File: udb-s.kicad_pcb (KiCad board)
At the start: 4 copper layers, 40 x 9 mm, 11 parts, among them J1 TYPE-C-31-M-12, J2 78171-0004, U1 TPD4E05U06DQAR

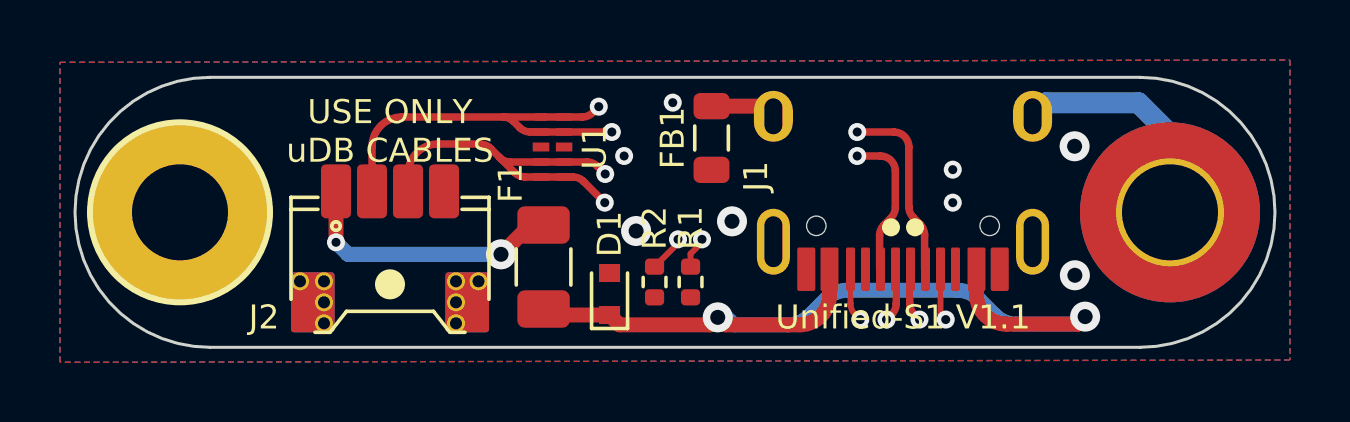
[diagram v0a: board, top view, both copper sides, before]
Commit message: Changed the Pinout of the ezMate connector. Added panelization with KiKit. 2x5 panels is about as small as possible for PCBA at JLCPCB, they want 70x70mm minimal size of the PCB. This means 50 PCBs is the MOQ with 5 panels.
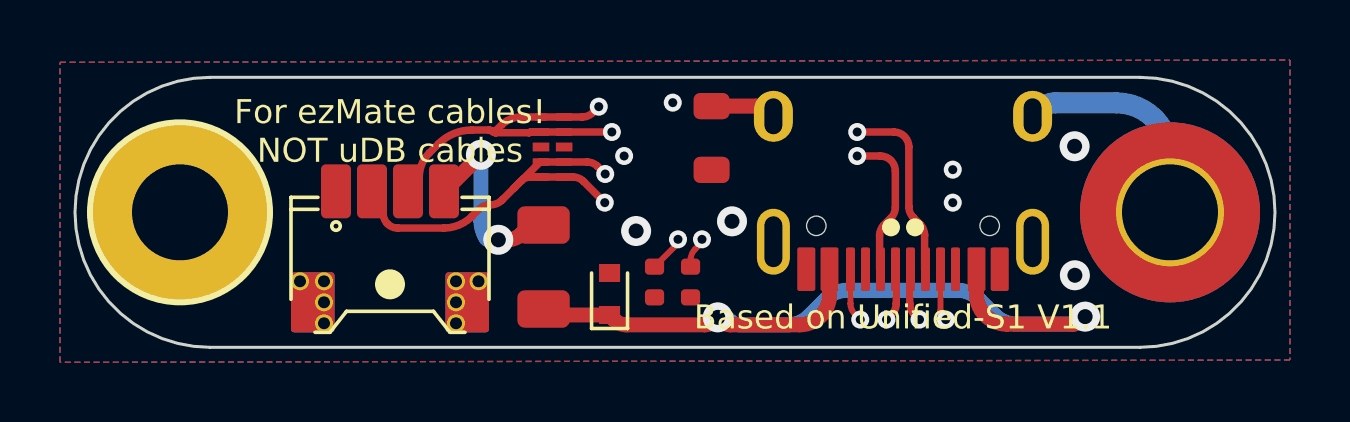
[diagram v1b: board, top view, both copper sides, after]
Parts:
- removed G***: LOGO, locallib:UnifiedLogo
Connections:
- J2 pad 1: 5V -> GND
- J2 pad 2: D- -> D+
- J2 pad 3: D+ -> D-
- J2 pad 4: GND -> 5V
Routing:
- net 5V: track 9.19 -> 6.63 mm
- net D-: track 49.5 -> 47.9 mm
- net D+: track 49.6 -> 50.4 mm
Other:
- board text added: "Based on Unified-S1 V1.1"
- board text added: "Based on Unified-S1 V1.1 But for use with off-the-shelf {dblquote}flipped{dblquote} ezMate-cables: Pin1 is Pin4 on the other end. NOT ACCORDING TO uDB-Spec"
- board text added: "For ezMate cables! NOT uDB cables"
- board text removed: "USE ONLY uDB CABLES"
- board text removed: "Unified-S1 V1.1"
- board text removed: "Unified-S1 V1.1 www.unified- daughterboard.github.io"
